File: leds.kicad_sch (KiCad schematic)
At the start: 2 parts, among them J21 Conn_01x02, U4 TC4427

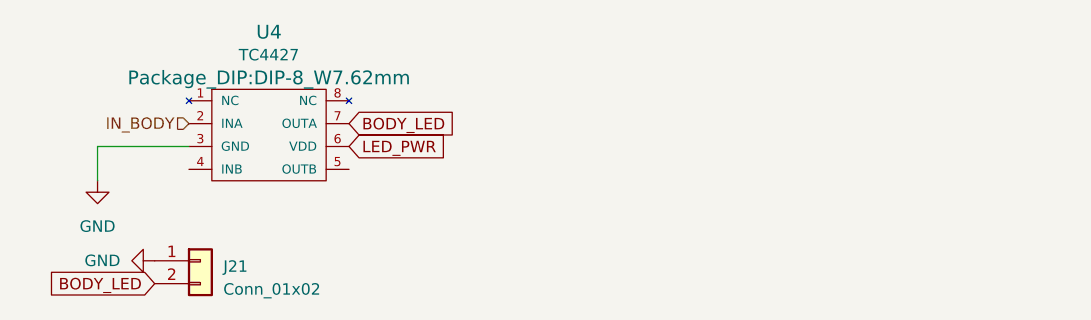
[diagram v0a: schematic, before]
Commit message: initial relocation of pca, re-order servo connectors
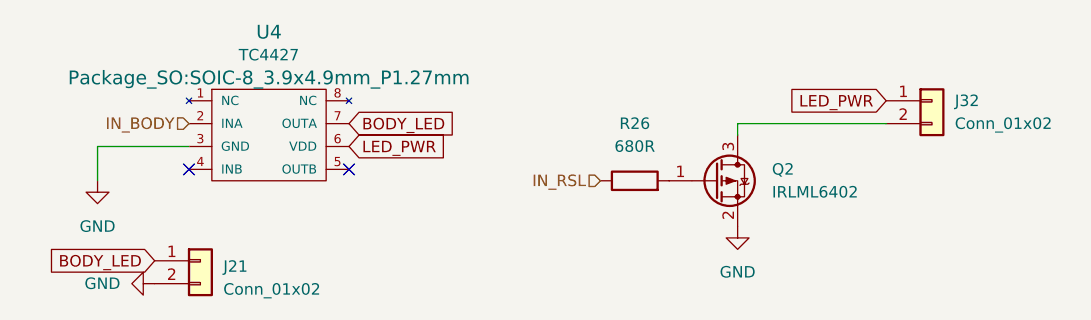
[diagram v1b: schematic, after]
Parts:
- added J32: Conn_01x02, Connector_JST:JST_XH_B2B-XH-A_1x02_P2.50mm_Vertical, symbol Connector_Generic:Conn_01x02
- added Q2: IRLML6402, Package_TO_SOT_SMD:SOT-23, symbol Transistor_FET:IRLML6402
- added R26: 680R, Resistor_SMD:R_0603_1608Metric, symbol Device:R
- J21: Part Number (none) -> B2B-XH-A
- U4: footprint Package_DIP:DIP-8_W7.62mm -> Package_SO:SOIC-8_3.9x4.9mm_P1.27mm; Part Number (none) -> TC4427ACOA713
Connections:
- net BODY_LED: now also J21.1 (Pin_1); no longer J21.2 (Pin_2)
- net GND: now also J21.2 (Pin_2), Q2.2 (S); no longer J21.1 (Pin_1)
- net LED_PWR: now also J32.1 (Pin_1)
- new net: Q2.1 (G), R26.2
- new net: J32.2 (Pin_2), Q2.3 (D)
- new net IN_RSL: R26.1
- no-connect marks 0 -> 2
